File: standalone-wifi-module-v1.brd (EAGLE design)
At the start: 26.9 x 26.6 mm, 29 parts, among them J1 USB (No Data), U1 ESP12SMD, U2 MCP73833-UN, U3 XC9140, U4 MCP1703CB

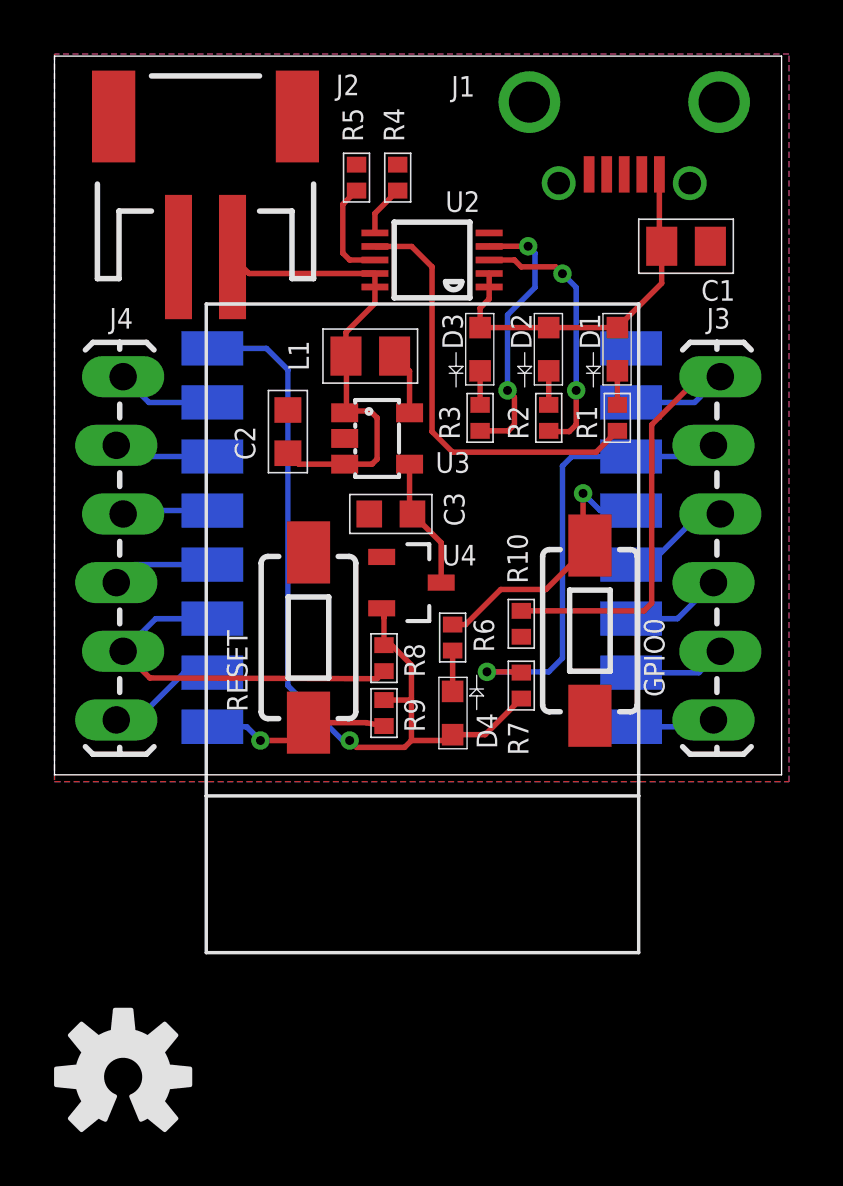
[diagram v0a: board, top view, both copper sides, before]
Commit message: Ordered boards from OSH Park, updated full BOM in README.
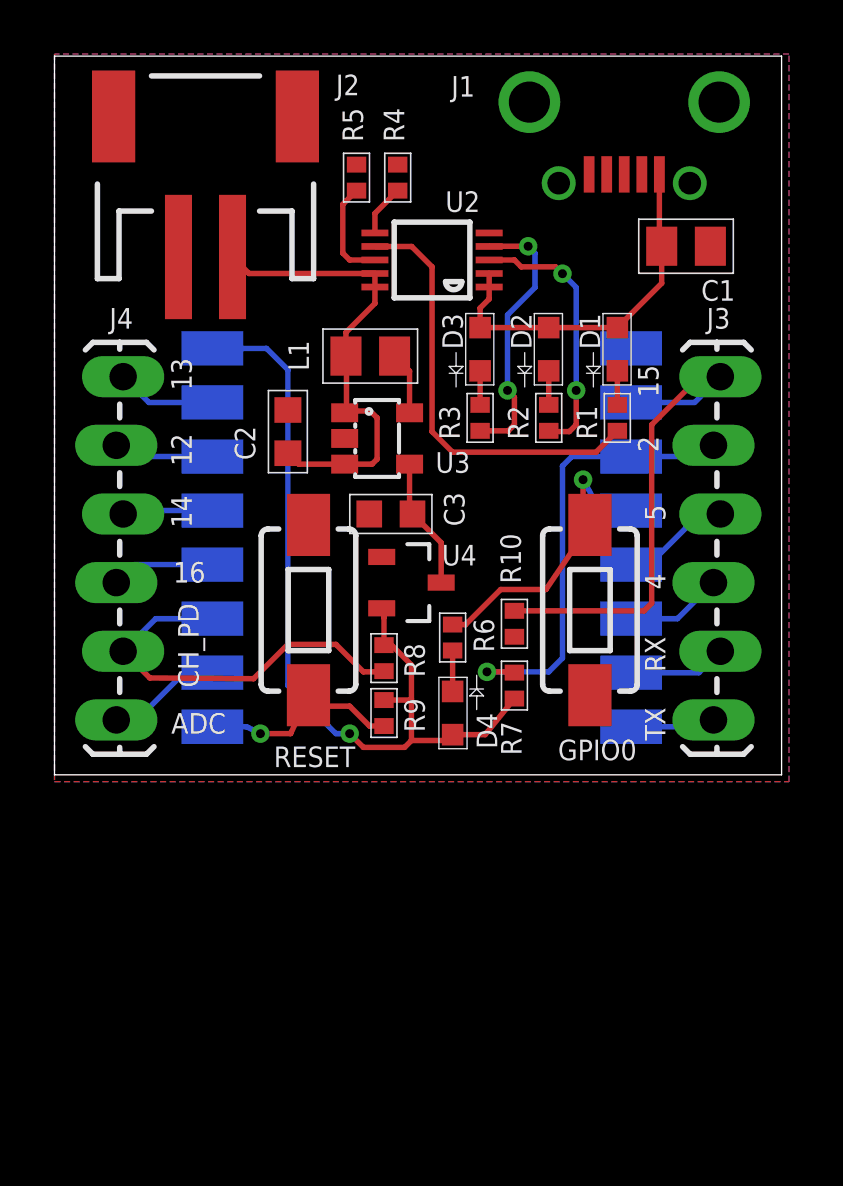
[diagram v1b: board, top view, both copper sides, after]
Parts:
- moved U$2 33.7 mm to (5.59, 22.4), flipped to the bottom
- moved RESET 1.02 mm to (9.40, 6.10)
- moved GPIO0 0.76 mm to (19.8, 6.10)
- moved R10 0.25 mm to (17.0, 5.59)
- moved R7 0.25 mm to (17.0, 3.30)
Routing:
- net GPIO0: track 10.4 -> 12.1 mm
- net !RESET: track 6.85 -> 7.79 mm
- net CH_PD: track 14.0 -> 14.8 mm
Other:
- board text added: "12"
- board text added: "13"
- board text added: "14"
- board text added: "15"
- board text added: "16"
- board text added: "2"
- board text added: "4"
- board text added: "5"
- board text added: "ADC"
- board text added: "CH_PD"
- board text added: "RX"
- board text added: "TX"
- board text added: "WIFI MODULE Wickerbox 2015-Sep-15 CERN OHL v1.2"
